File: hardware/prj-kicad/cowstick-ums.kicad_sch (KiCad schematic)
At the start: 12 parts, among them J1 CONN_USB-A, U2 LM3671, U90 AZ2210

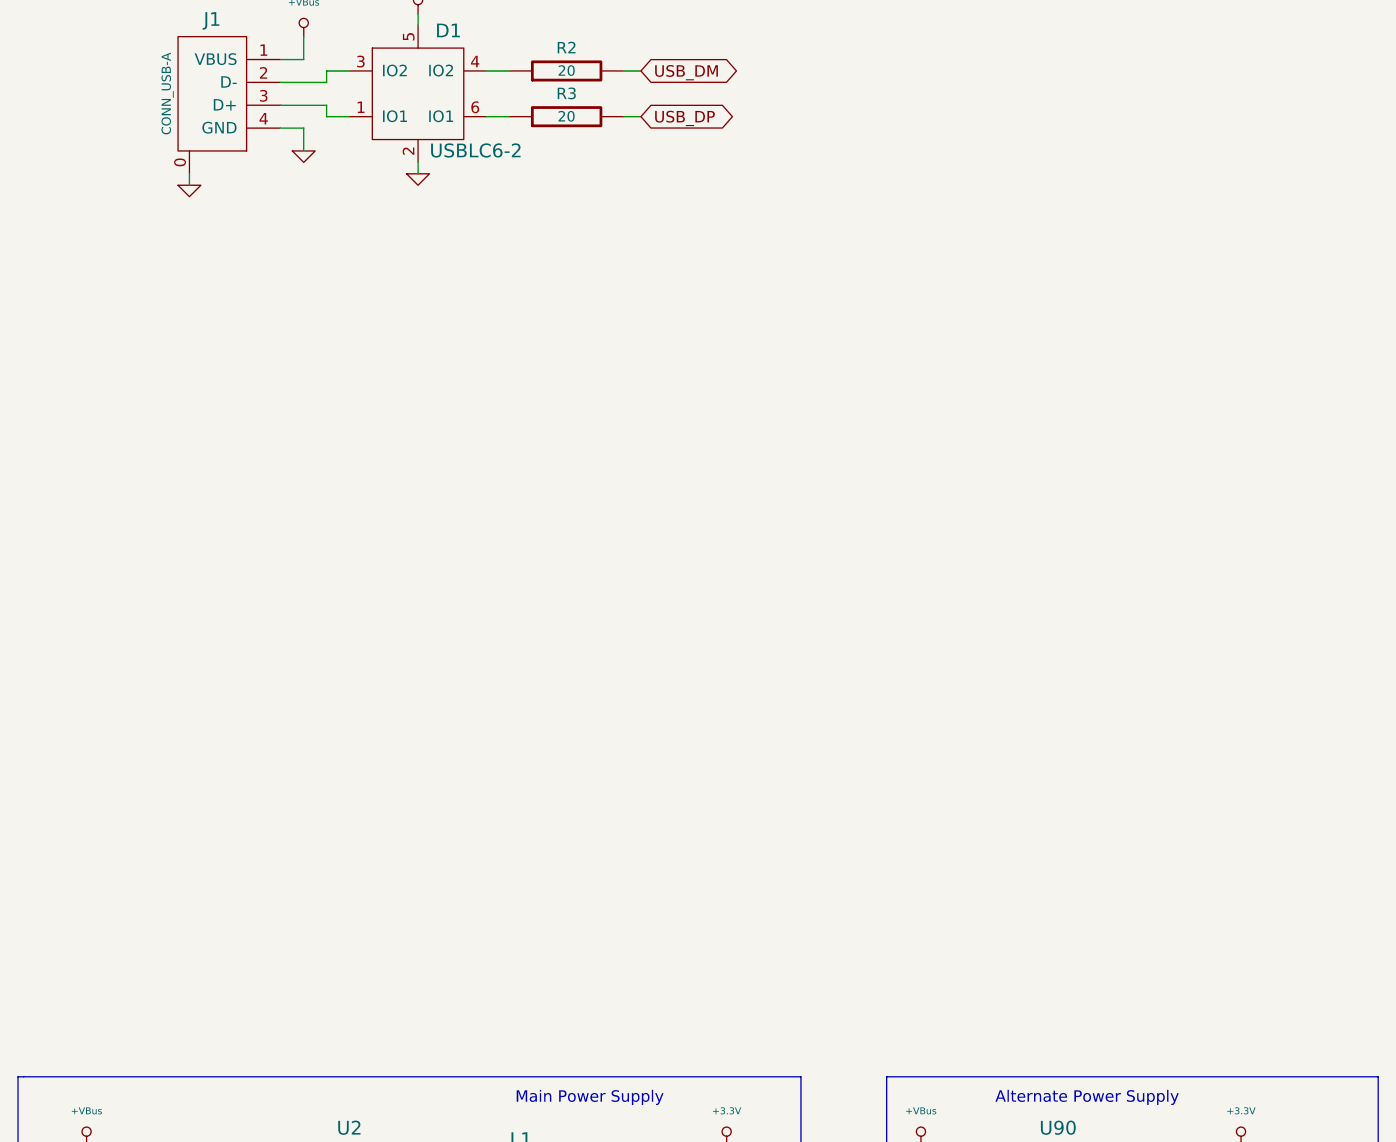
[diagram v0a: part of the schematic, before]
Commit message: Hardware: Improve PCB r1, add MCU (STM32G0)
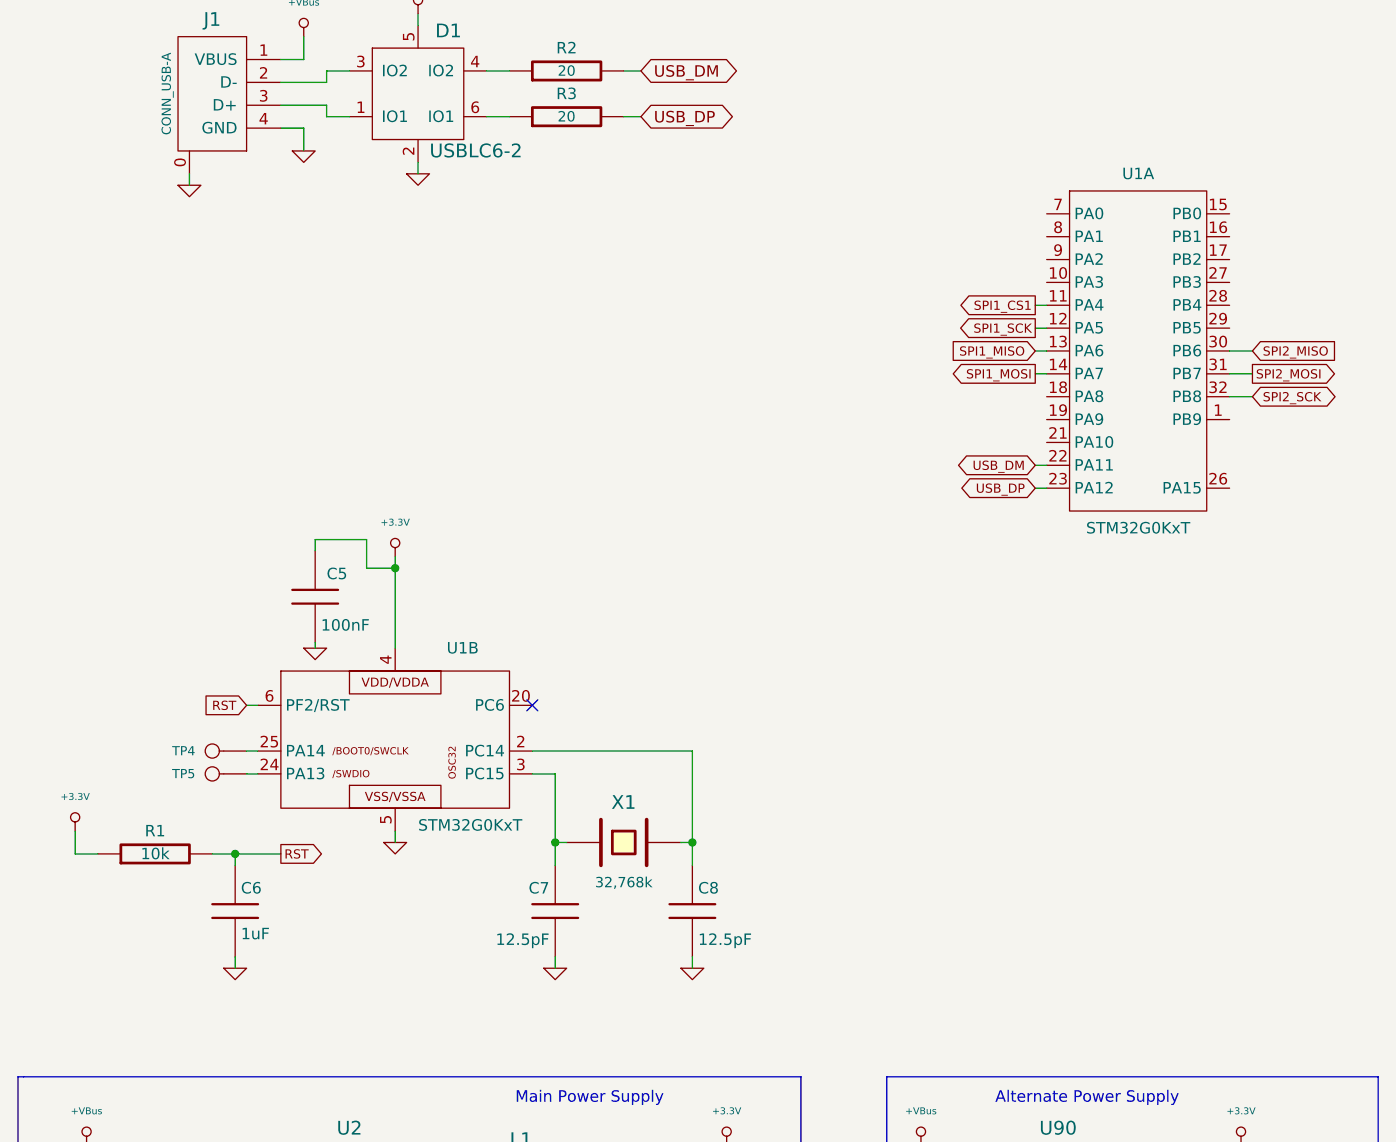
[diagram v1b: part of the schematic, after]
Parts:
- added C5: 100nF, cowstick-ums:C_0603, symbol cowstick-ums:C
- added C6: 1uF, cowstick-ums:C_0603, symbol cowstick-ums:C
- added C7, C8: 12.5pF, cowstick-ums:C_0603, symbol cowstick-ums:C
- added R1: 10k, cowstick-ums:R_0603, symbol cowstick-ums:R
- added TP4, TP5: CONN_1, symbol cowstick-ums:CONN_1
- added U1: STM32G0KxT, cowstick-ums:TQFP32, symbol cowstick-ums:STM32G0KxT
- added X1: 32,768k, cowstick-ums:Q_3.2x1.5, symbol cowstick-ums:CRYSTAL
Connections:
- net +3.3V: now also C5.1, R1.1, U1.4
- net GND: now also C5.2, C6.2, C7.2, C8.2, U1.5
- net USB_DM: now also U1.22 (PA11)
- net USB_DP: now also U1.23 (PA12)
- new net: C8.1, U1.2 (PC14), X1.2
- new net: TP5.1, U1.24 (PA13)
- new net: TP4.1, U1.25 (PA14)
- new net: C7.1, U1.3 (PC15), X1.1
- new net RST: C6.1, R1.2, U1.6 (PF2/RST)
- new net SPI1_CS1: U1.11 (PA4)
- new net SPI1_MISO: U1.13 (PA6)
- new net SPI1_MOSI: U1.14 (PA7)
- new net SPI1_SCK: U1.12 (PA5)
- new net SPI2_MISO: U1.30 (PB6)
- new net SPI2_MOSI: U1.31 (PB7)
- new net SPI2_SCK: U1.32 (PB8)
- no-connect marks 0 -> 1

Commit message: Hardware: Improve PCB r1, add two SOIC8 flash memory ic for channel 1
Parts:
- added C10, C9: 100nF, cowstick-ums:C_0603, symbol cowstick-ums:C
- added U3, U4: W25QxxVSN, cowstick-ums:SOIC-8, symbol cowstick-ums:W25QxxVSN
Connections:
- net +3.3V: now also C10.1, C9.1, U3.8, U4.8
- net GND: now also C10.2, C9.2, U3.4, U4.4
- net SPI1_CS1: now also U3.1 (CS)
- net SPI1_MISO: now also U3.2 (IO1_DO), U4.2 (IO1_DO)
- net SPI1_MOSI: now also U3.5 (IO0_DI), U4.5 (IO0_DI)
- net SPI1_SCK: now also U3.6 (CLK), U4.6 (CLK)
- net SPI1_CS2: now reaches U1.16 (PB1)
- net SPI1_CS2: now also U4.1 (CS)
- net SPI1_WP: now reaches U1.17 (PB2)
- net SPI1_WP: now also U3.3 (IO2_WP), U4.3 (IO2_WP)
- net SPI1_HLD: now reaches U1.18 (PA8)
- net SPI1_HLD: now also U3.7 (IO3_HOLD), U4.7 (IO3_HOLD)
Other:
- note added: "Memory #1 (with 2 slots)"
- note added: "Slot1"
- note added: "Slot2"

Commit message: Hardware: Improve PCB r1, add one Nand flash memory for "large" capacity (channel 2)
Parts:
- added C11: 100nF, cowstick-ums:C_0603, symbol cowstick-ums:C
- added U5: W25NxxVZE, cowstick-ums:WSON8, symbol cowstick-ums:W25NxxVZE
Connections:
- net +3.3V: now also C11.1, U5.8
- net GND: now also C11.2, U5.4
- net SPI2_MISO: now also U5.2 (IO1_DO)
- net SPI2_MOSI: now also U5.5 (IO0_DI)
- net SPI2_SCK: now also U5.6 (CLK)
- net SPI2_CS: now reaches U1.1 (PB9)
- net SPI2_CS: now also U5.1 (CS)
- net SPI2_HLD: now reaches U1.27 (PB3)
- net SPI2_HLD: now also U5.7 (IO3_HOLD)
- net SPI2_WP: now reaches U1.28 (PB4)
- net SPI2_WP: now also U5.3 (IO2_WP)
- no-connect marks 1 -> 10
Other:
- note added: "Memory #2 (NAND)"

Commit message: Hardware: Finish and cleanup pcb r1 and create production files
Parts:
- added D2: LED, cowstick-ums:C_0805, symbol cowstick-ums:LED
- added R4: 330, cowstick-ums:R_0603, symbol cowstick-ums:R
- added TP1, TP2, TP3: CONN_1, cowstick-ums:TP_SMD, symbol cowstick-ums:CONN_1
- added TP6, TP7, TP8, TP9: CONN_1, cowstick-ums:TP_PIN, symbol cowstick-ums:CONN_1
- TP4, TP5: footprint (none) -> cowstick-ums:TP_SMD
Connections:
- net +3.3V: now also R4.2, TP1.1
- net GND: now also TP2.1, TP6.1, TP9.1
- net RST: now also TP3.1
- net SWD_IO: now reaches TP5.1, U1.24 (PA13)
- net SWD_CLK: now reaches TP4.1, U1.25 (PA14)
- net UART_RX: now reaches U1.10 (PA3)
- net UART_RX: now also TP8.1
- net LED: now reaches U1.29 (PB5)
- net LED: now also D2.2 (K)
- net UART_TX: now reaches U1.9 (PA2)
- net UART_TX: now also TP7.1
- new net: D2.1 (A), R4.1
- no-connect marks 10 -> 7
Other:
- note added: "Processor"
- note added: "Test and Debug"
- note added: "USB Interface"
- moved on the sheet: C10, C11, C5, C6, C7, C8, C9, D1, J1, R1, R2, R3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

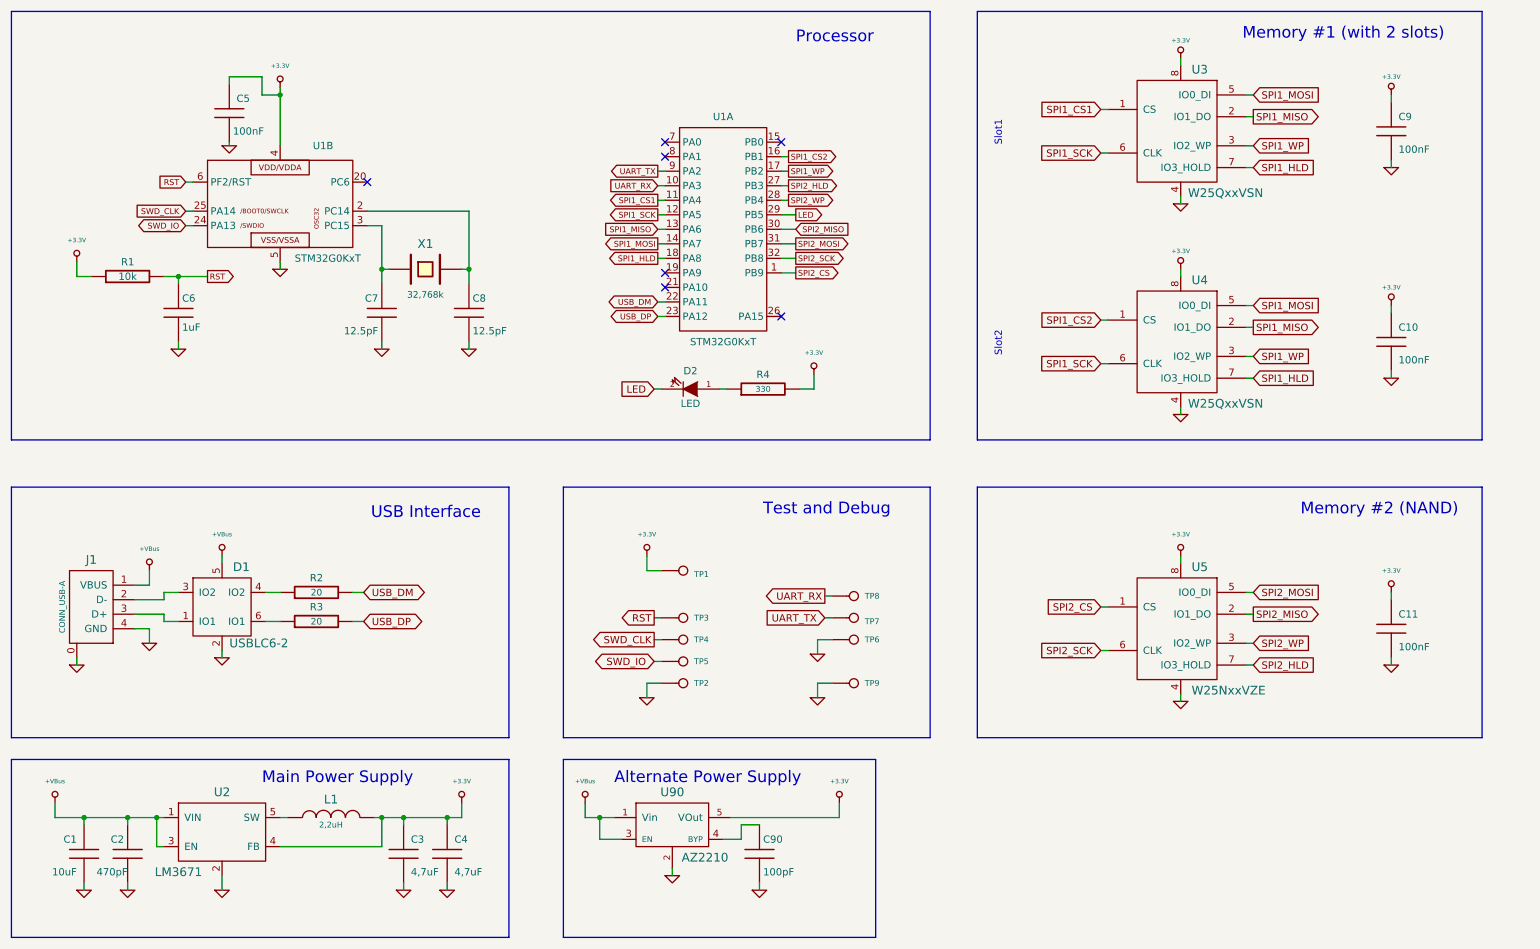
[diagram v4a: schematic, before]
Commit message: Hardware: Modify PCB for a new revision (rev2) and create production files  - Add pushbutton and a second LED  - Replace power reg and USB connector with a new refs
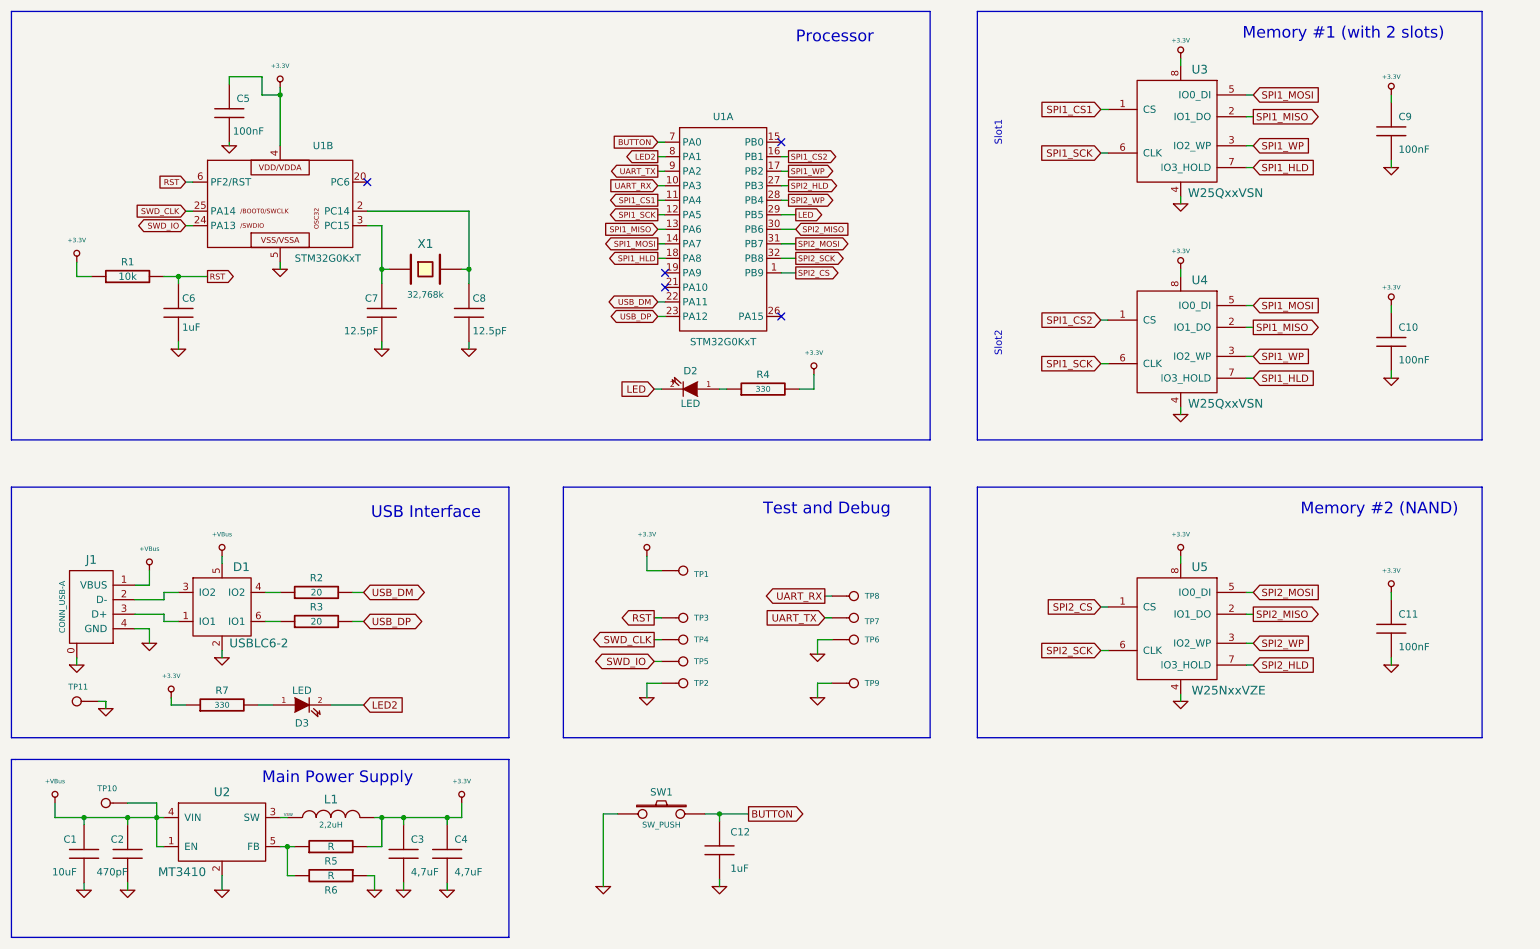
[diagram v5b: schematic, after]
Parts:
- removed C90: 100pF, cowstick-ums:C_0603, symbol cowstick-ums:C
- removed U2: LM3671, cowstick-ums:SOT23-5, symbol cowstick-ums:LM3671
- removed U90: AZ2210, cowstick-ums:SOT23-5, symbol cowstick-ums:AZ2210
- added C12: 1uF, cowstick-ums:C_0603, symbol cowstick-ums:C
- added D3: LED, cowstick-ums:C_0805, symbol cowstick-ums:LED
- added R5, R6: R, cowstick-ums:R_0603, symbol cowstick-ums:R
- added R7: 330, cowstick-ums:R_0603, symbol cowstick-ums:R
- added SW1: SW_PUSH, cowstick-ums:BUT_TC029, symbol cowstick-ums:SW_PUSH
- added TP10, TP11: CONN_1, cowstick-ums:TP_SMD, symbol cowstick-ums:CONN_1
- added U2: MT3410, cowstick-ums:SOT23-5, symbol cowstick-ums:MT3410
- J1: footprint cowstick-ums:CONN_MC32604 -> cowstick-ums:CONN_AM90YC
- L1: footprint cowstick-ums:I_CDRH2D14 -> cowstick-ums:I_SMD_3x3
- TP1: footprint cowstick-ums:TP_SMD -> cowstick-ums:TP_SMD2
- TP7, TP8: footprint cowstick-ums:TP_PIN -> cowstick-ums:TP_SMD
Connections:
- net +3.3V: now also R5.2, R7.1
- net +VBus: now also TP10.1, U2.1 (EN), U2.4 (VIN)
- net GND: now also C12.2, R6.1, SW1.1, TP11.1, U2.2
- net VSW: now reaches L1.1
- net VSW: now also U2.3 (SW)
- net BUTTON: now reaches U1.7 (PA0)
- net BUTTON: now also C12.1, SW1.2
- net LED2: now reaches U1.8 (PA1)
- net LED2: now also D3.2 (K)
- new net: R5.1, R6.2, U2.5 (FB)
- new net: D3.1 (A), R7.2
- no-connect marks 7 -> 5
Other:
- note removed: "Alternate Power Supply"
